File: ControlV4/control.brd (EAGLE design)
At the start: 51.7 x 54.6 mm, 49 parts, among them P1 CONNEC_1X03, P10 CONNEC_1X03, P11 CONNEC_1X03, P12 CONNEC_1X03, P2 CONNEC_1X03, P3 CONNEC_1X03, P4 CONNEC_1X03, P5 CONNEC_1X03, P6 CONNEC_1X03, P7 CONNEC_1X03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

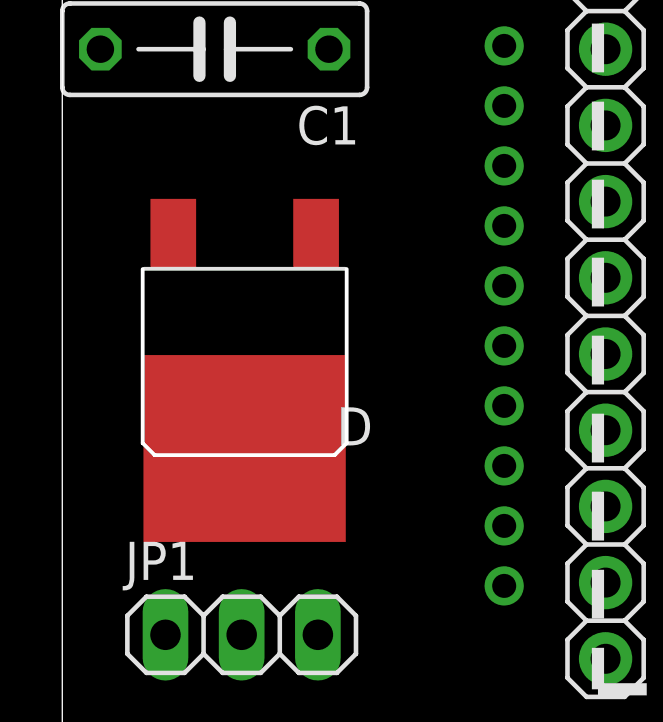
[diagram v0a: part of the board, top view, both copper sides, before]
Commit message: Moving to official package for diode
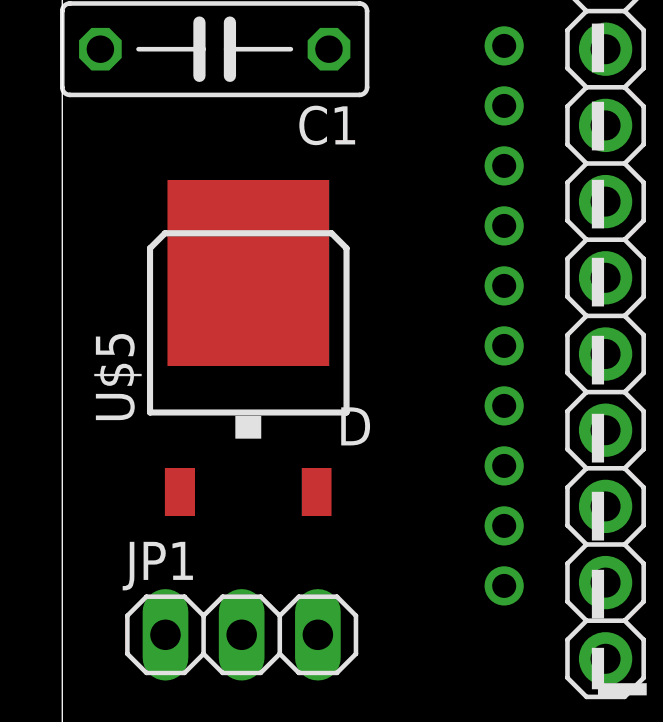
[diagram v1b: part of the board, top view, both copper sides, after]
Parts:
- removed U$12: (no value), RobotCampus:D-PAK
- added U$5: DIODETO252AA, RobotCampus:TO-252AA
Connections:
- net NET1: now also U$5.4; no longer U$12.OUT
- net VCC_IN: now also U$5.3; no longer U$12.IN
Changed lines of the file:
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@@
 <attribute name="OC_FARNELL" value="1337916" x="51.13" y="34.29" size="1.778" layer="28" rot="MR180" display="off"/>
 </element>
-<element name="U$12" library="RobotCampus" package="D-PAK" value="" x="6.08" y="12.43" rot="R180"/>
 <element name="JP1" library="pinhead" package="1X03" value="" x="5.98" y="3.34"/>
 <element name="U$2" library="RobotCampus" package="CONNEC_1X03" value="CONNEC_1X03" x="3.81" y="50.8"/>
@@
 <attribute name="OC_FARNELL" value="1439518" x="28.5" y="42.8" size="1.778" layer="28" rot="MR0" display="off"/>
 </element>
+<element name="U$5" library="RobotCampus" package="TO-252AA" value="DIODETO252AA" x="6.2" y="12.9"/>
 </elements>
 <signals>
@@
 <wire x1="39.97" y1="10.86" x2="49.53" y2="11.43" width="0" layer="19" extent="1-1"/>
 <wire x1="39.87" y1="16.91" x2="39.97" y2="10.86" width="0" layer="19" extent="1-1"/>
-<wire x1="24.14" y1="31.75" x2="39.87" y2="16.91" width="0" layer="19" extent="16-16"/>
+<wire x1="29.4398" y1="41.6062" x2="49.53" y2="40.64" width="0" layer="19" extent="16-16"/>
+<wire x1="23.67" y1="44" x2="29.4398" y2="41.6062" width="0" layer="19" extent="16-16"/>
+<wire x1="18.11" y1="48.26" x2="23.67" y2="44" width="0" layer="19" extent="1-1"/>
+<wire x1="10.16" y1="50.8" x2="18.11" y2="48.26" width="0" layer="19" extent="1-1"/>
+<wire x1="7.62" y1="52.07" x2="10.16" y2="50.8" width="0" layer="19" extent="1-1"/>
+<wire x1="3.08" y1="42.45" x2="7.62" y2="52.07" width="0" layer="19" extent="1-1"/>
+<wire x1="24.14" y1="31.75" x2="29.4398" y2="41.6062" width="0" layer="19" extent="16-16"/>
+<wire x1="3.08" y1="29.75" x2="3.08" y2="42.45" width="0" layer="19" extent="1-1"/>
+<wire x1="1.27" y1="22.86" x2="3.08" y2="29.75" width="0" layer="19" extent="1-1"/>
 <wire x1="14.73" y1="22.97" x2="24.14" y2="31.75" width="0" layer="19" extent="16-16"/>
-<wire x1="1.27" y1="22.86" x2="14.73" y2="22.97" width="0" layer="19" extent="1-1"/>
-<wire x1="3.08" y1="29.75" x2="1.27" y2="22.86" width="0" layer="19" extent="1-1"/>
-<wire x1="3.08" y1="42.45" x2="3.08" y2="29.75" width="0" layer="19" extent="1-1"/>
-<wire x1="7.62" y1="52.07" x2="3.08" y2="42.45" width="0" layer="19" extent="1-1"/>
-<wire x1="10.16" y1="50.8" x2="7.62" y2="52.07" width="0" layer="19" extent="1-1"/>
-<wire x1="18.11" y1="48.26" x2="10.16" y2="50.8" width="0" layer="19" extent="1-1"/>
-<wire x1="23.67" y1="44" x2="18.11" y2="48.26" width="0" layer="19" extent="1-1"/>
-<wire x1="29.4398" y1="41.6062" x2="1.27" y2="22.86" width="0" layer="19" extent="1-1"/>
 </signal>
 <signal name="PWM7">
@@
 <contactref element="JST_IN" pad="VCC"/>
 <contactref element="JP1" pad="1"/>
-<contactref element="U$12" pad="IN"/>
 <contactref element="R13" pad="1"/>
+<contactref element="U$5" pad="3"/>
 <wire x1="3.08" y1="33.75" x2="29.22" y2="31.75" width="0" layer="19" extent="1-16"/>
-<wire x1="3.7" y1="16.73" x2="3.08" y2="33.75" width="0" layer="19" extent="1-1"/>
-<wire x1="3.44" y1="3.34" x2="3.7" y2="16.73" width="0" layer="19" extent="1-1"/>
+<wire x1="8.48" y1="8.1" x2="3.08" y2="33.75" width="0" layer="19" extent="1-1"/>
+<wire x1="3.44" y1="3.34" x2="8.48" y2="8.1" width="0" layer="19" extent="1-1"/>
 </signal>
 <signal name="NET1">
-<contactref element="U$12" pad="OUT"/>
 <contactref element="JP1" pad="3"/>
-<wire x1="8.52" y1="3.34" x2="6.08" y2="9.55" width="0" layer="19" extent="1-1"/>
+<contactref element="U$5" pad="4"/>
+<wire x1="8.52" y1="3.34" x2="6.2" y2="15.4" width="0" layer="19" extent="1-1"/>
 </signal>
 <signal name="VMICRO" class="1">
@@
 <contactref element="C3" pad="1"/>
 <contactref element="U$4" pad="3"/>
-<wire x1="12.7" y1="43.18" x2="12.7" y2="50.8" width="0" layer="19" extent="1-1"/>
+<wire x1="12.7" y1="43.18" x2="28.5" y2="43.9938" width="0" layer="19" extent="16-16"/>
+<wire x1="12.7" y1="50.8" x2="12.7" y2="43.18" width="0" layer="19" extent="1-1"/>
 <wire x1="3.08" y1="46.45" x2="12.7" y2="43.18" width="0" layer="19" extent="1-1"/>
-<wire x1="42.41" y1="16.91" x2="12.7" y2="43.18" width="0" layer="19" extent="1-1"/>
+<wire x1="42.41" y1="16.91" x2="28.5" y2="43.9938" width="0" layer="19" extent="16-16"/>
 <wire x1="33.35" y1="2.54" x2="42.41" y2="16.91" width="0" layer="19" extent="1-1"/>
-<wire x1="28.5" y1="43.9938" x2="33.35" y2="2.54" width="0" layer="19" extent="1-1"/>
 </signal>
 <signal name="N$13">
@@
 <contactref element="C6" pad="1"/>
 <contactref element="U$4" pad="2"/>
-<wire x1="27.5602" y1="41.6062" x2="23.67" y2="41.46" width="0" layer="19" extent="1-1"/>
+<wire x1="23.67" y1="41.46" x2="27.5602" y2="41.6062" width="0" layer="19" extent="16-16"/>
 </signal>
 </signals>

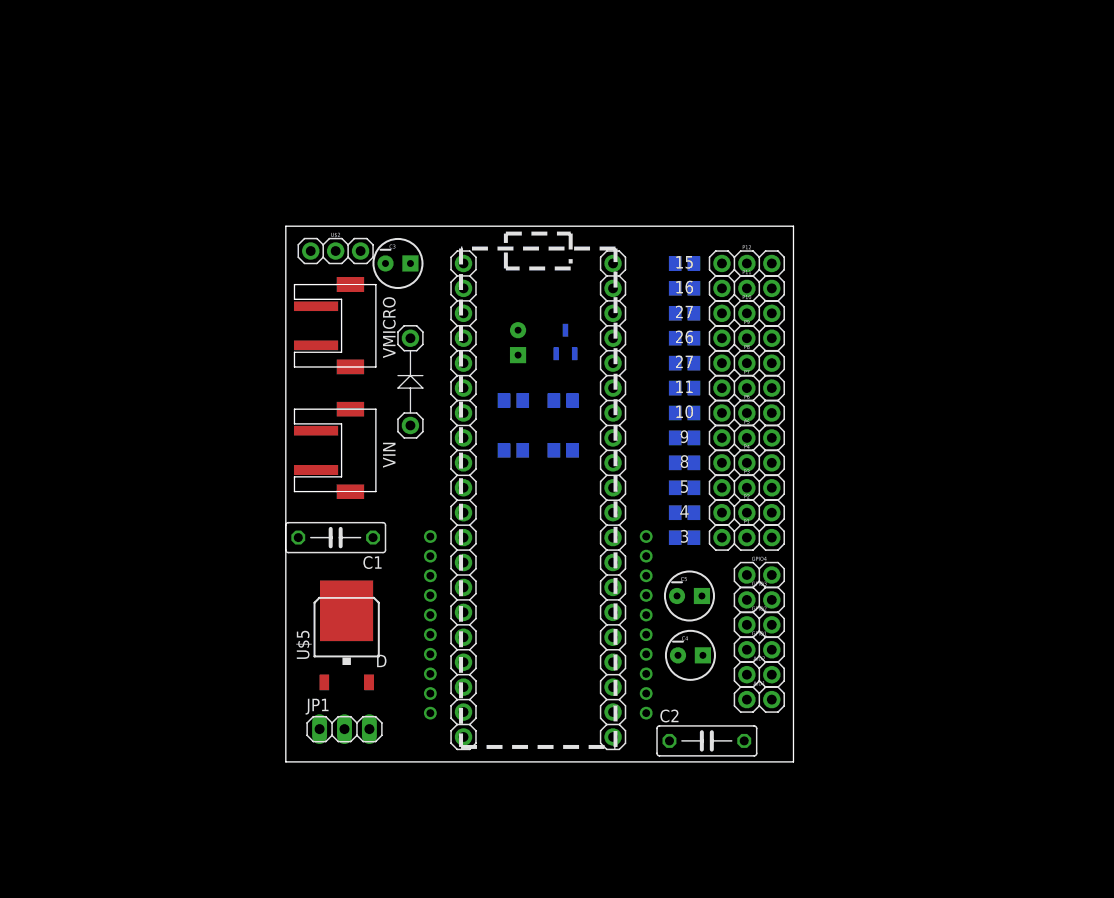
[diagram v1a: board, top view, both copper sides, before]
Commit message: First version full autorouted
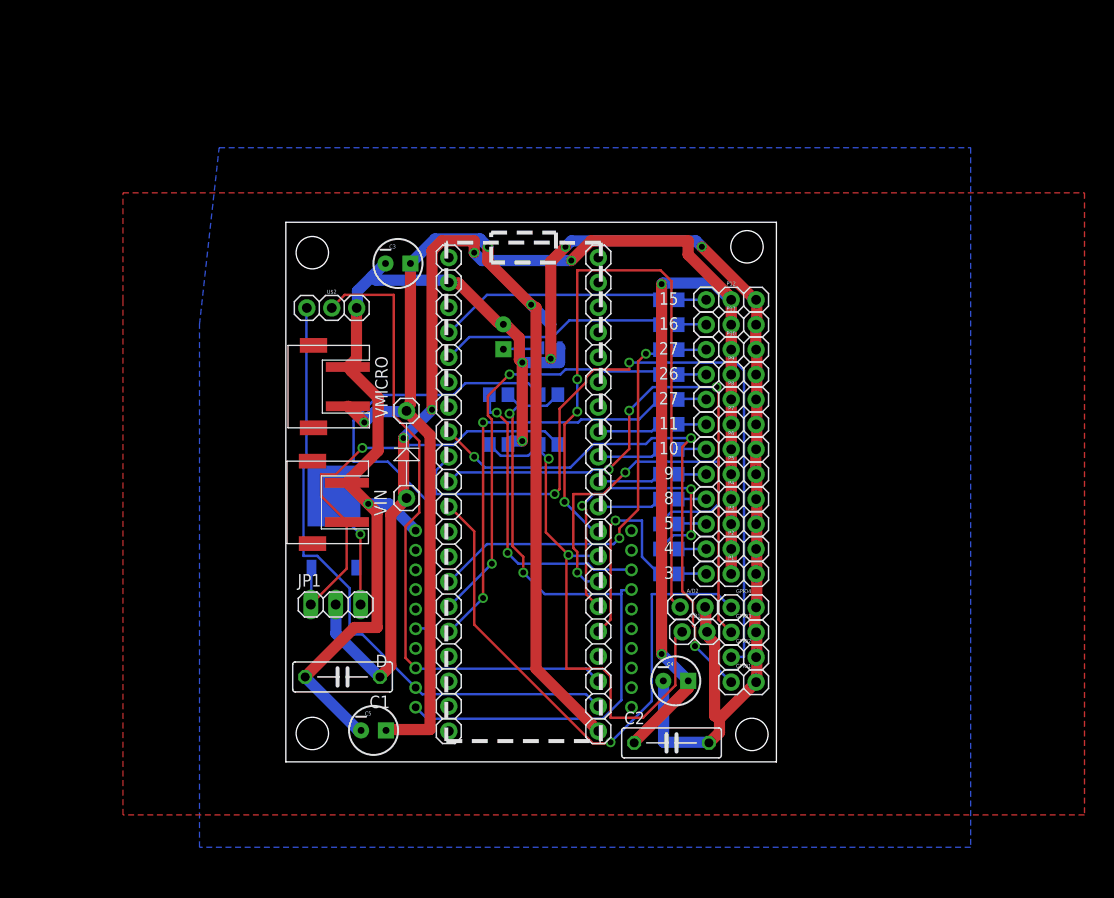
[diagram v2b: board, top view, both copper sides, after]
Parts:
- added U$6, U$7, U$8, U$9: (no value), RobotCampus:STAND-OFF
- moved C5 35.0 mm to (8.94, 3.21)
- moved C1 14.2 mm to (5.78, 8.66)
- moved JP1 12.7 mm to (5.08, 16.0)
- moved U$5 11.8 mm to (4.90, 24.6), flipped to the bottom
- moved A/D2 9.69 mm to (41.5, 14.5)
- moved A/D1 9.55 mm to (41.7, 12.0)
- moved U$3 7.41 mm to (12.3, 26.9)
- moved JST_MICRO 6.25 mm to (4.32, 38.2), turned to 180 degrees
- moved U$2 5.81 mm to (3.41, 45.0)
- moved JST_IN 5.37 mm to (4.22, 26.4), turned to 180 degrees
- moved P10 4.03 mm to (44.1, 40.8)
- moved P11 4.03 mm to (44.1, 43.3)
- moved P12 4.03 mm to (44.1, 45.8)
- moved P3 4.03 mm to (44.1, 23.0)
- moved R10 4.03 mm to (39.0, 39.5)
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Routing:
- net GND: track 0.00 -> 206.5 mm, vias 0 -> 6
- net VPOWER: track 0.00 -> 177.7 mm, vias 0 -> 6
- net VMICRO: track 0.00 -> 126.5 mm, vias 0 -> 3
- net D2: track 0.00 -> 77.6 mm, vias 0 -> 2
- net A2: track 0.00 -> 72.5 mm, vias 0 -> 3
- net 33: track 0.00 -> 69.5 mm, vias 0 -> 2
- net MTX: track 0.00 -> 66.2 mm
- net MRX: track 0.00 -> 64.5 mm
- net D3: track 0.00 -> 59.2 mm, vias 0 -> 3
- net D4: track 0.00 -> 57.6 mm, vias 0 -> 1
- net A1: track 0.00 -> 56.8 mm, vias 0 -> 2
- net D1: track 0.00 -> 54.7 mm, vias 0 -> 3
- net N$13: track 0.00 -> 48.4 mm
- net VCC_IN: track 0.00 -> 46.2 mm, vias 0 -> 1
- net PWM9: track 0.00 -> 42.3 mm, vias 0 -> 2
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- added copper zone on layer 1, net GND
- added copper zone on layer 16, net GND
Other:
- board size 51.7 x 54.6 mm -> 50 x 55 mm

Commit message: V4
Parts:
- removed JP1: (no value), pinhead:1X03
- added C7, C8: (no value), SparkFun-Capacitors:CPOL-RADIAL-10UF-25V
- added JP: CONNEC_1X03, RobotCampus:CONNEC_1X03
- XB1: value XBEE-PRO -> XBEE; device maxstream:XBEE-PRO -> RobotCampus:XBEE
- moved U$3 6.24 mm to (11.6, 33.1)
- moved U$4 4.20 mm to (27.0, 39.2)
- moved XB1 3.61 mm to (23.9, 18.2)
- moved C6 2.86 mm to (21.6, 40.5)
- moved R15 2.40 mm to (26.9, 35.0)
- moved R16 2.30 mm to (21.8, 35.1)
- moved C3 1.02 mm to (10.4, 50.6)
- moved C1 0.67 mm to (5.48, 9.26)
- moved U$2 0.60 mm to (2.81, 45.0)
- moved U$1 0.36 mm to (32.0, 51.7)
- moved C5 0.22 mm to (8.74, 3.11)
- moved R9 0.20 mm to (39.2, 42.0)
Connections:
- net 3.3: now also C8.1
- net GND: now also C7.2, C8.2
- net NET1: now also JP.1; no longer JP1.3
- net VCC_IN: now also JP.3; no longer JP1.1
- net VPOWER: now also C7.1, JP.2; no longer JP1.2
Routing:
- net GND: track 206.5 -> 0.00 mm, vias 6 -> 0
- net VPOWER: track 177.7 -> 0.00 mm, vias 6 -> 0
- net VMICRO: track 126.5 -> 0.00 mm, vias 3 -> 0
- net D2: track 77.6 -> 0.00 mm, vias 2 -> 0
- net A2: track 72.5 -> 0.00 mm, vias 3 -> 0
- net 33: track 69.5 -> 0.00 mm, vias 2 -> 0
- net MTX: track 66.2 -> 0.00 mm
- net MRX: track 64.5 -> 0.00 mm
- net D3: track 59.2 -> 0.00 mm, vias 3 -> 0
- net D4: track 57.6 -> 0.00 mm, vias 1 -> 0
- net A1: track 56.8 -> 0.00 mm, vias 2 -> 0
- net D1: track 54.7 -> 0.00 mm, vias 3 -> 0
- net N$13: track 48.4 -> 0.00 mm
- net VCC_IN: track 46.2 -> 0.00 mm, vias 1 -> 0
- net PWM9: track 42.3 -> 0.00 mm, vias 2 -> 0
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- removed copper zone on layer 1, net GND
- removed copper zone on layer 16, net GND
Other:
- board text added: "25"

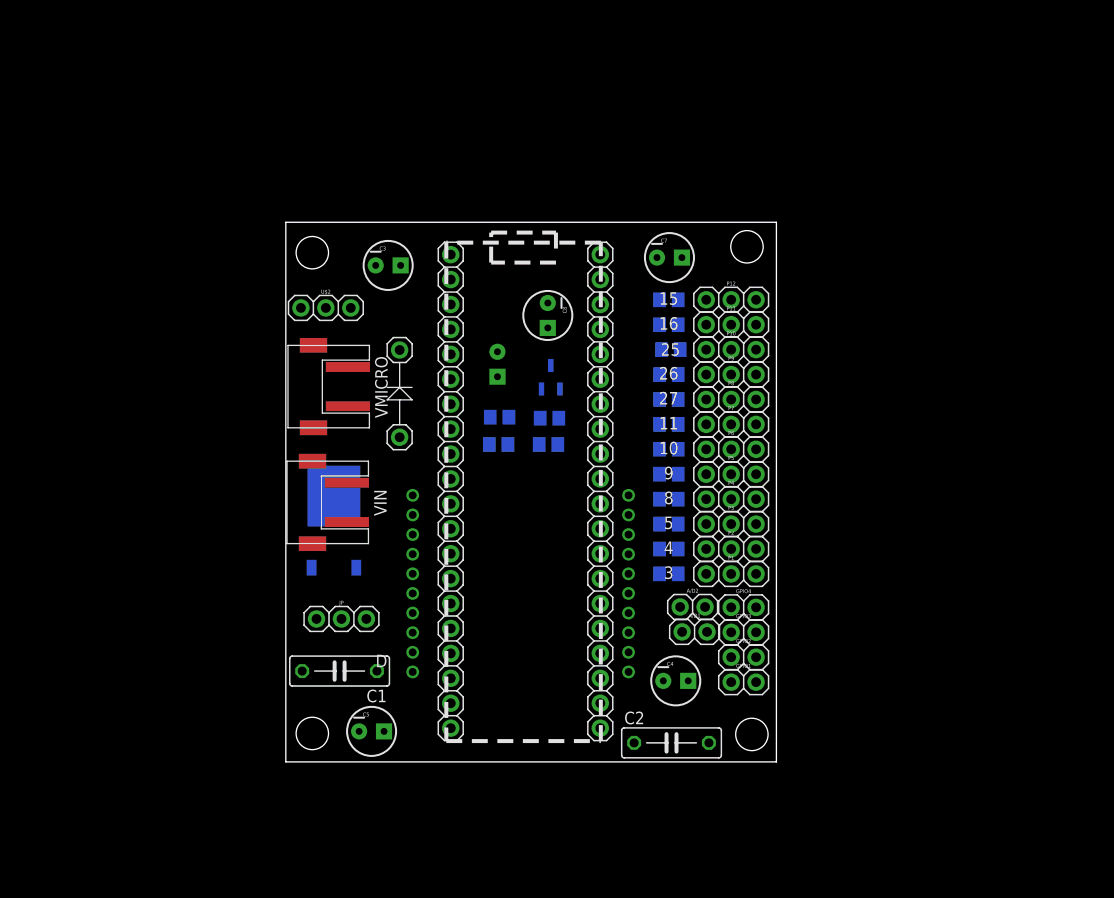
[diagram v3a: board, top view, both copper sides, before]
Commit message: Ajout du logo sérigraphié
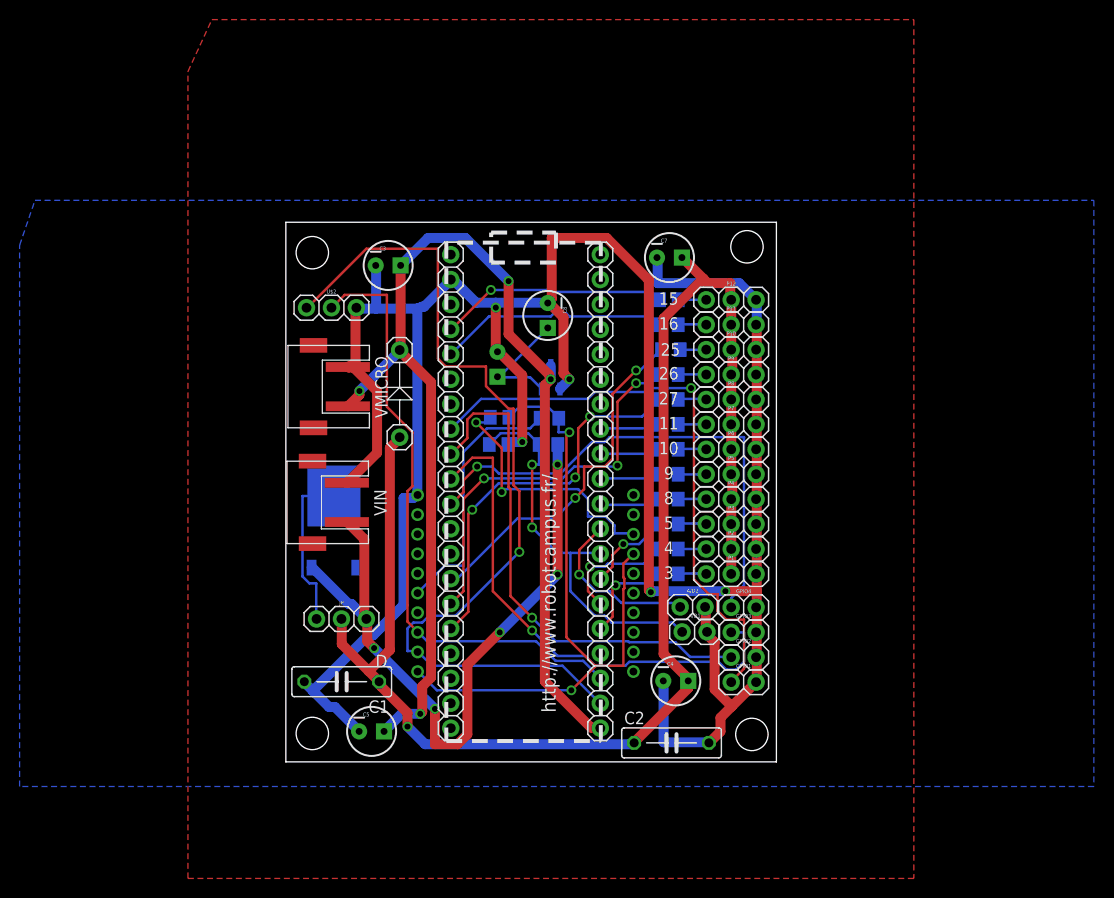
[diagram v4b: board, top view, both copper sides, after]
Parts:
- moved C1 1.11 mm to (5.69, 8.18)
- moved U$2 0.57 mm to (3.38, 45.0)
- moved XB1 0.50 mm to (24.4, 18.2)
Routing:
- net GND: track 0.00 -> 271.1 mm, vias 0 -> 5
- net VPOWER: track 0.00 -> 150.9 mm, vias 0 -> 1
- net VMICRO: track 0.00 -> 125.6 mm, vias 0 -> 4
- net MRX: track 0.00 -> 91.7 mm, vias 0 -> 1
- net VCC_IN: track 0.00 -> 71.2 mm, vias 0 -> 5
- net 33: track 0.00 -> 68.5 mm, vias 0 -> 2
- net MTX: track 0.00 -> 62.9 mm
- net D1: track 0.00 -> 60.5 mm, vias 0 -> 1
- net D3: track 0.00 -> 52.7 mm, vias 0 -> 1
- net D2: track 0.00 -> 52.4 mm, vias 0 -> 1
- net D4: track 0.00 -> 51.9 mm, vias 0 -> 1
- net A1: track 0.00 -> 40.3 mm, vias 0 -> 2
- net PWM9: track 0.00 -> 40.3 mm, vias 0 -> 3
- net PWM8: track 0.00 -> 39.6 mm, vias 0 -> 3
- net PWM10: track 0.00 -> 36.3 mm, vias 0 -> 2
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- added copper zone on layer 1, net GND
- added copper zone on layer 16, net GND
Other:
- board text added: "/tmp/robotcampus.bmp"
- board text added: "http://www.robotcampus.fr/"

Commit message: V4
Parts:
- removed JST_IN, JST_MICRO: JST_2, perso:JST_2
- added U$10, U$11: JST_2, RobotCampus:JST_2
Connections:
- net GND: now also U$10.GND, U$11.GND; no longer JST_IN.GND, JST_MICRO.GND
- net VCC_IN: now also U$11.VCC; no longer JST_IN.VCC
- net VMICRO: now also U$10.VCC; no longer JST_MICRO.VCC
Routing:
- net GND: track 271.1 -> 253.8 mm
- net VMICRO: track 125.6 -> 128.6 mm
- net MRX: track 91.7 -> 89.7 mm
- net 3.3: track 12.2 -> 11.2 mm
- net VCC_IN: track 71.2 -> 72.1 mm
- net N$15: track 26.8 -> 26.0 mm
- net PWM10: track 36.3 -> 35.8 mm
- net 33: track 68.5 -> 68.0 mm
